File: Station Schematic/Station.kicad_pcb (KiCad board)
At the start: 2 copper layers, 178.7 x 124.3 mm, 204 parts, among them J1 Conn_01x02, J10 ~220, J11 TABLE_HV F, J12 Conn_01x02, J13 ENC1, J14 ENC2, J15 ENC2, J16 AC 12V, J17 Conn_01x02, J18 Conn_01x02, J19 Conn_01x02, J2 OLED_Out_PCB, J20 Conn_01x02, J21 Conn_01x05 M, J22 Motor 24V, J23 Termistor M, J24 Reley_Control, J25 Reley_Control, J26 Reley24V, J3 ENC1, J4 ~220, J40 RV3 M, J5 FAN_HV F, J6 FAN_Control, J7 FAN_Control, J8 TABLE_Control, J9 TABLE_Control, K1 Relay_SPDT, Q1 STD10PF06, Q10 IRF740, Q11 BC847B, Q2 BC847B, Q3 BC857B, Q4 BC847, Q5 BT139-600, Q6 BC847B, Q7 BT139-600, Q8 NPN, Q9 NoName, SW1 RotaryEncoder_Switch, SW2 SW_Push, SW3 SW_Push, SW4 RotaryEncoder_Switch, SW5 SW_Push, SW6 SW_Push, SW7 SW_Push, SW8 SW_Push, U1 TL431LP, U2 LM358, U3 MOC3041M, U4 LM358, U5 LM358, U6 MOC3041M, U7 LM358, U8 BluePill_STM32F103C8T6

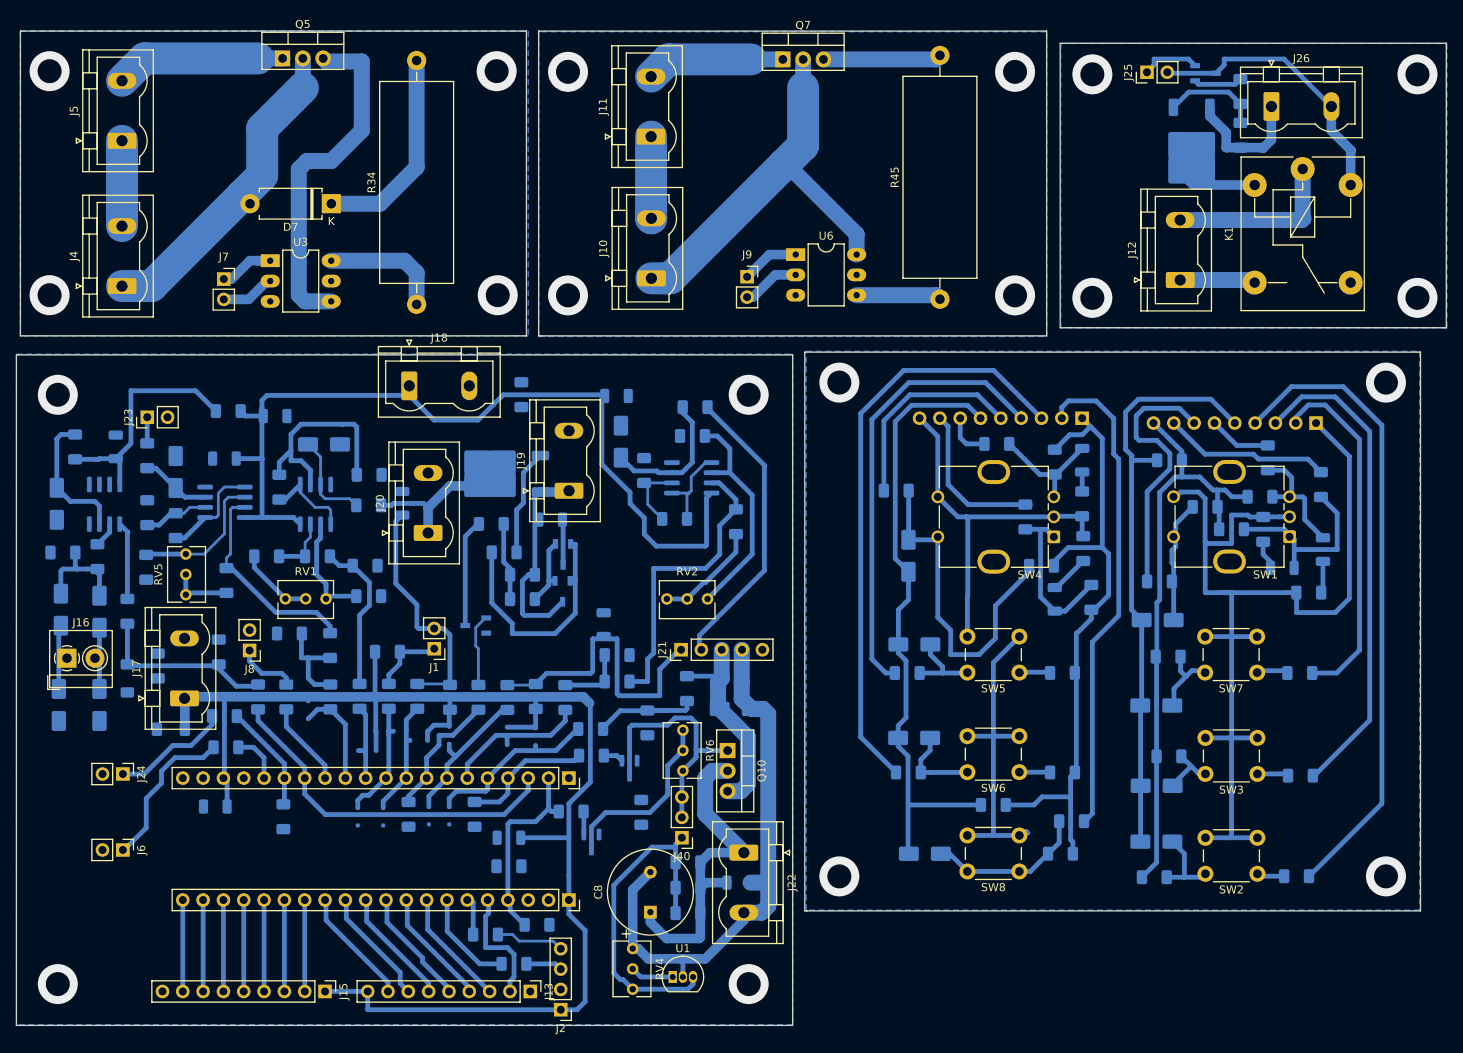
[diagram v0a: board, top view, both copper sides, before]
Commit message: PAC was changed
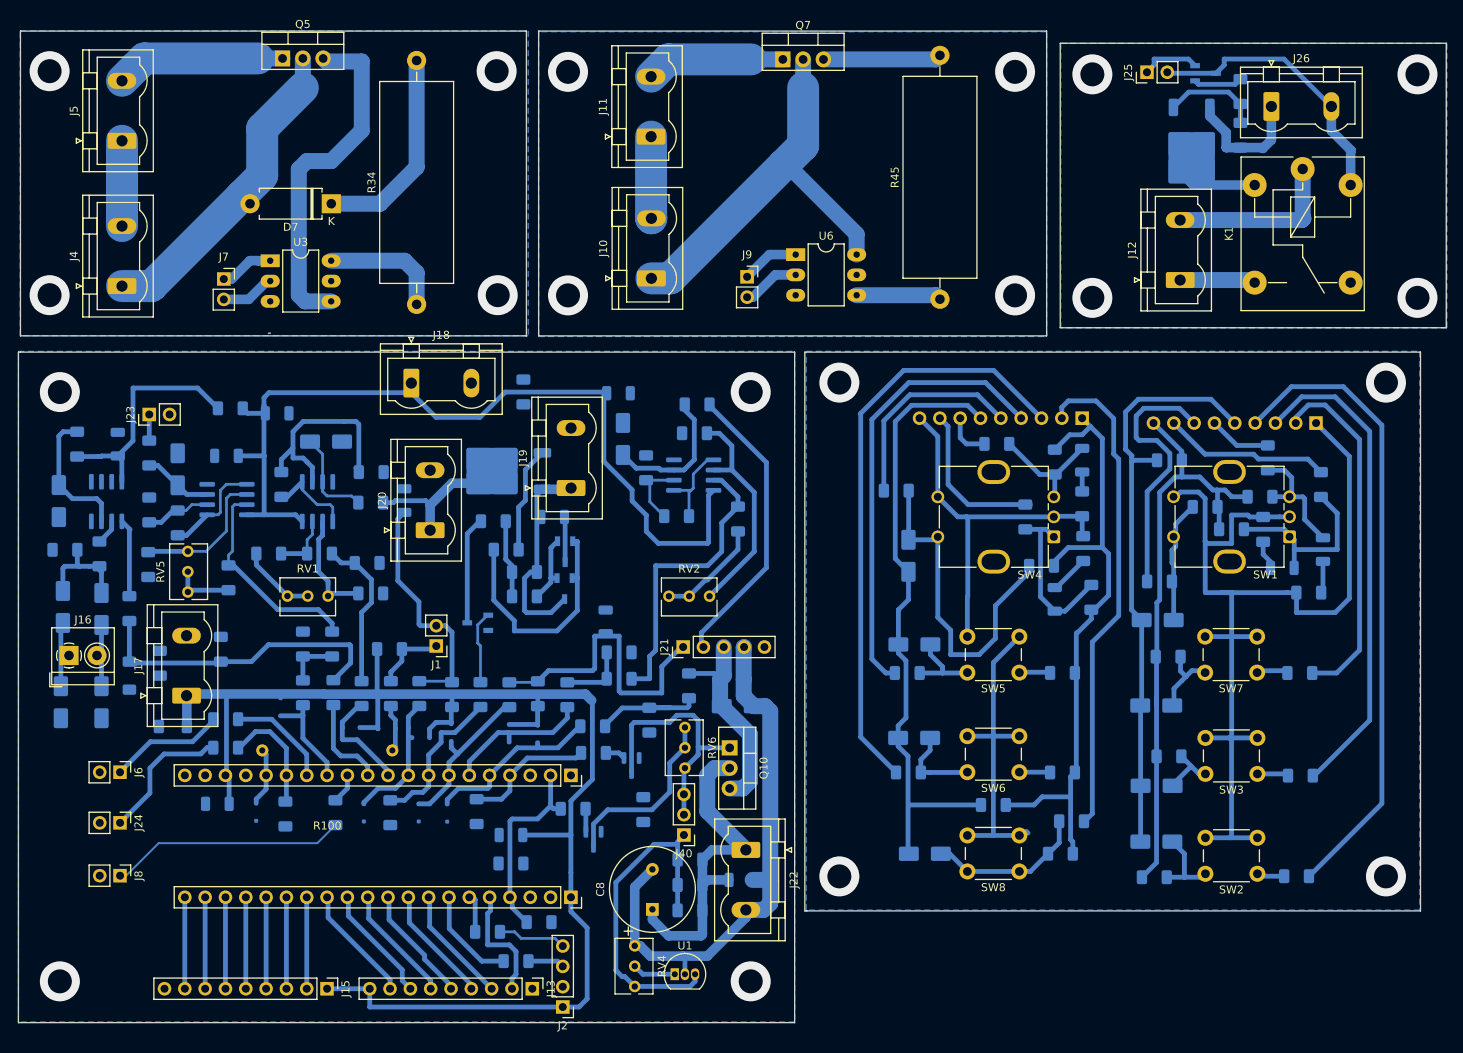
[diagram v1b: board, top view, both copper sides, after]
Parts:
- added R100: 0R, Den_Castom_lib:R0 16.128, F.Cu at (62.5, 108.5)
- moved J8 32.5 mm to (36.6, 124.1), turned to -90 degrees
- moved R44 15.7 mm to (63.5, 116.2), turned to -90 degrees
- moved D26 12.7 mm to (53.6, 116.2)
- moved J6 9.72 mm to (36.6, 111.2)
- moved R88 9.43 mm to (63.2, 101.2)
- moved J24 6.11 mm to (36.6, 117.5)
- moved R76 3.94 mm to (49.8, 108.1)
- moved D25 3.52 mm to (65.5, 105.6)
- moved R28 3.51 mm to (49.8, 104.6)
- moved D2 3.48 mm to (56.6, 103.0)
- moved R43 3.47 mm to (59.4, 101.3)
- moved D28 2.46 mm to (67.1, 116.2)
- moved R69 2.30 mm to (70.4, 116.2)
- moved R42 2.14 mm to (59.4, 95.2), turned to 90 degrees
- moved D30 1.32 mm to (73.9, 116.2)
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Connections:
- D9 pad 2: /MController/Vibration_Detection -> Net-(D9-A)
- R54 pad 1: /MController/Vibration_Detection -> Net-(D9-A)
- U8 pad 10: /MController/Vibration_Detection -> /MController/Solder_Analog
- U8 pad 11: /MController/Solder_Analog -> /MController/ZCD
- U8 pad 12: /MController/TABLE_Analog -> /MController/TABLE_Control+
- U8 pad 13: /MController/TABLE_Control+ -> /MController/TABLE_Analog
- U8 pad 14: /MController/ZCD -> /MController/FAN_Control+
- U8 pad 16: /MController/FAN_Control+ -> /MController/Vibration_Detection
- U8 pad 3: /MController/ZCD -> unconnected-(U8-C14-Pad3)
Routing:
- net /MController/ZCD: track 44.6 -> 11.8 mm
- net Net-(J8-Pin_1): track 8.21 -> 29.5 mm
- net Net-(D24-K): track 22.3 -> 38.3 mm
- net /MController/Vibration_Detection: track 15.8 -> 7.37 mm
- net Net-(D9-A): track 0.00 -> 7.02 mm
- net /MController/TABLE_Control+: track 10.5 -> 3.73 mm
- net /MController/FAN_Control+: track 6.30 -> 13.0 mm
- net Net-(R41-Pad2): track 12.3 -> 7.07 mm
- net Net-(J6-Pin_1): track 19.8 -> 14.5 mm
- net /MController/Solder_Analog: track 9.89 -> 13.3 mm
- net /MController/SOLDER_PWM: track 16.4 -> 19.4 mm
- net Net-(J24-Pin_1): track 14.6 -> 17.4 mm
- net /MController/Solder_Full_Power: track 14.7 -> 16.9 mm
- net /FAN/Gerkon: track 18.4 -> 19.9 mm
- net /MController/Reley_Control: track 13.5 -> 14.6 mm
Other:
- board size 178.7 x 124.3 mm -> 178.5 x 124 mm
